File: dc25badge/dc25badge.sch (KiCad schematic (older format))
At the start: 37 parts, among them P1 BATT, P2 USB_OTG, P3 CORTEX, Q1 DMN1019USN, SW1 RESET, SW3 MODE, SW4 BRIGHT, U1 MIC5305, U2 TPS61232, U3 ATSAMD21E18A-AU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

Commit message: Update board.
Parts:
- added C23, C28: NP, Capacitors_SMD:C_0805, symbol C_Small
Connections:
- net +5V: now also C23.1
- net GND: now also C23.2, C28.2
- net VBAT: now also C28.1
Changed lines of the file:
@@
 	950  850  950  2400
 Wire Wire Line
-	950  850  1200 850
+	700  850  1200 850
 Connection ~ 1200 850
 Connection ~ 950  1750
@@
 Connection ~ 4150 2550
 Wire Wire Line
-	2850 2550 5650 2550
+	2850 2550 5900 2550
 Wire Wire Line
 	3600 2550 3600 2400
@@
 $EndComp
 Wire Wire Line
-	4600 1850 4700 1850
-Wire Wire Line
-	4700 1850 4700 1400
+	4700 1850 4600 1850
+Wire Wire Line
+	4700 1400 4700 1850
 Wire Wire Line
 	4700 1400 4300 1400
@@
 Connection ~ 4900 2550
 Wire Wire Line
-	4600 1950 5650 1950
-Wire Wire Line
 	5400 1950 5400 2200
 Wire Wire Line
@@
 Connection ~ 4700 1950
 Wire Wire Line
-	4900 2200 4900 1950
+	4900 1950 4900 2200
 Connection ~ 4900 1950
 Wire Wire Line
-	5150 2200 5150 1950
+	5150 1950 5150 2200
 Connection ~ 5150 1950
 Connection ~ 5400 1950
@@
 Wire Wire Line
 	7550 5300 7700 5300
+$Comp
+L C_Small C23
+U 1 1 593C3098
+P 5900 2300
+F 0 "C23" H 5950 2350 50  0000 L CNN
+F 1 "NP" H 5950 2200 50  0000 L CNN
+F 2 "Capacitors_SMD:C_0805" H 5900 2300 50  0001 C CNN
+F 3 "" H 5900 2300 50  0000 C CNN
+	1    5900 2300
+	1    0    0    -1
+$EndComp
+Connection ~ 5650 1950
+Connection ~ 5650 2550
+Wire Wire Line
+	4600 1950 5900 1950
+Wire Wire Line
+	5900 1950 5900 2200
+Wire Wire Line
+	5900 2550 5900 2400
+$Comp
+L C_Small C28
+U 1 1 593C40FA
+P 700 1500
+F 0 "C28" H 710 1570 50  0000 L CNN
+F 1 "NP" H 710 1420 50  0000 L CNN
+F 2 "Capacitors_SMD:C_0805" H 700 1500 50  0001 C CNN
+F 3 "" H 700 1500 50  0000 C CNN
+	1    700  1500
+	1    0    0    -1
+$EndComp
+Wire Wire Line
+	700  1400 700  850
+Connection ~ 950  850
+$Comp
+L GND #PWR026
+U 1 1 593C428E
+P 700 1700
+F 0 "#PWR026" H 700 1450 50  0001 C CNN
+F 1 "GND" H 700 1550 50  0000 C CNN
+F 2 "" H 700 1700 50  0000 C CNN
+F 3 "" H 700 1700 50  0000 C CNN
+	1    700  1700
+	1    0    0    -1
+$EndComp
+Wire Wire Line
+	700  1700 700  1600
 $EndSCHEMATC

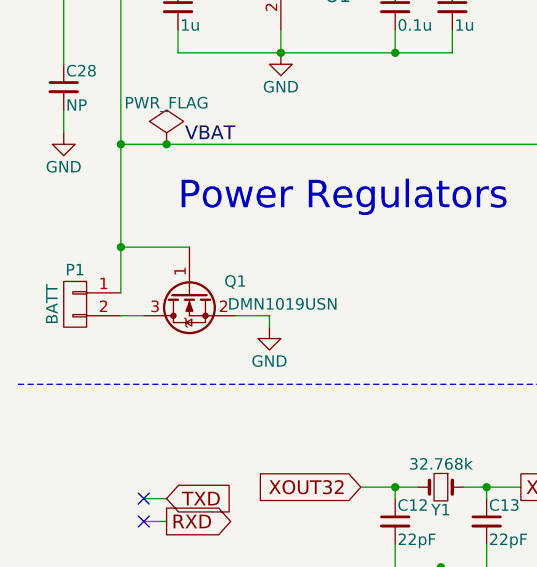
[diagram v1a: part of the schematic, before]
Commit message: Move components to not be in the way.
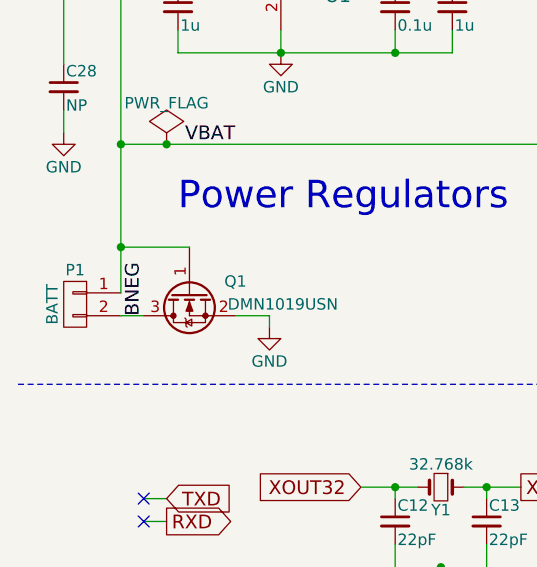
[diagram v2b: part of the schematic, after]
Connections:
- net BNEG: now reaches P1.2 (P2), Q1.3 (D)
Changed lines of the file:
@@
 EELAYER 25 0
 EELAYER END
-$Descr A4 11693 8268
+$Descr USLetter 11000 8500
 encoding utf-8
 Sheet 1 2
-Title ""
-Date ""
-Rev ""
-Comp ""
+Title "DC25 Badge XXV"
+Date "2017-06-24"
+Rev "2"
+Comp "@Matir"
 Comment1 ""
 Comment2 ""
@@
 Wire Wire Line
 	700  1700 700  1600
+Text Label 1050 2500 1    60   ~ 0
+BNEG
 $EndSCHEMATC

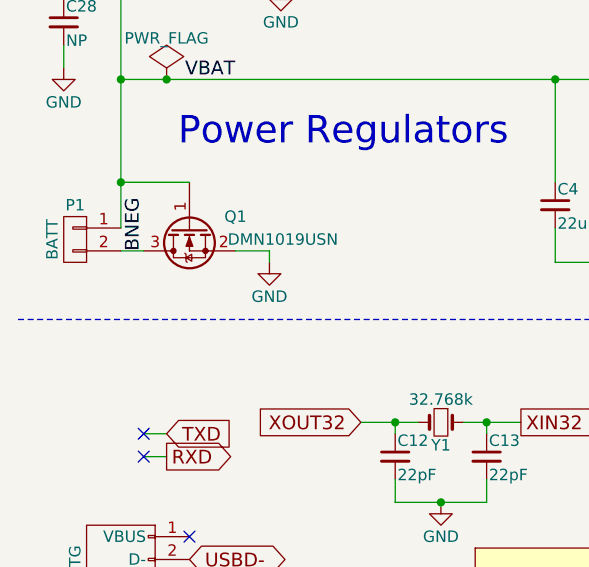
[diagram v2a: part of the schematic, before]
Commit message: Add jumper to bypass fet.
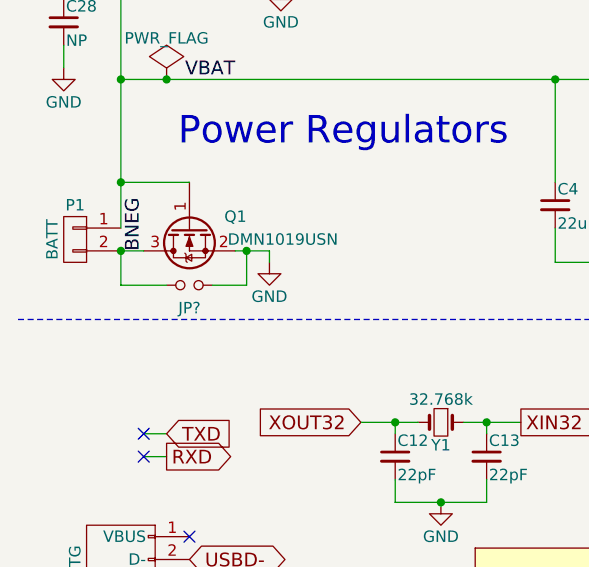
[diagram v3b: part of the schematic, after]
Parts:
- added JP?: Jumper_NO_Small, symbol Jumper_NO_Small
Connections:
- net BNEG: now also JP?.1
- net GND: now also JP?.2
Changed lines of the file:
@@
 Text Label 1050 2500 1    60   ~ 0
 BNEG
+$Comp
+L Jumper_NO_Small JP?
+U 1 1 594EF10E
+P 1250 2650
+F 0 "JP?" H 1250 2550 50  0000 C CNN
+F 1 "Jumper_NO_Small" H 1260 2590 50  0001 C CNN
+F 2 "" H 1250 2650 50  0000 C CNN
+F 3 "" H 1250 2650 50  0000 C CNN
+	1    1250 2650
+	1    0    0    -1
+$EndComp
+Wire Wire Line
+	1150 2650 950  2650
+Wire Wire Line
+	950  2650 950  2500
+Wire Wire Line
+	1350 2650 1500 2650
+Wire Wire Line
+	1500 2650 1500 2500
+Connection ~ 1500 2500
+Connection ~ 950  2500
 $EndSCHEMATC
